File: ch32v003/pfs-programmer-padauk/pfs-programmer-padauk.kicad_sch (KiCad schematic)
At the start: 26 parts, among them J1 PGM1, J2 PGM2, J3 PGM, J4 USB_C_Receptacle_USB2.0, J5 HOLE, J6 HOLE, Q1 SI2301CDS-T1-GE3, Q2 2n7002, Q3 SI2301CDS-T1-GE3, Q4 2n7002, U1 CH32V003F4U6, U3 XC6206P332

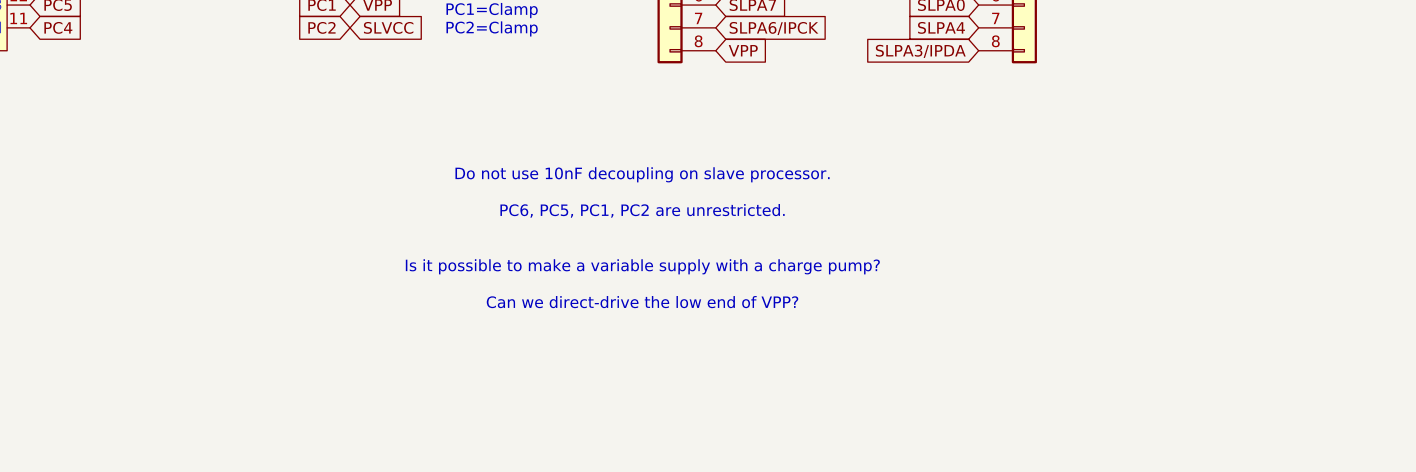
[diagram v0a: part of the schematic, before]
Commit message: Update with notes about charge pumps
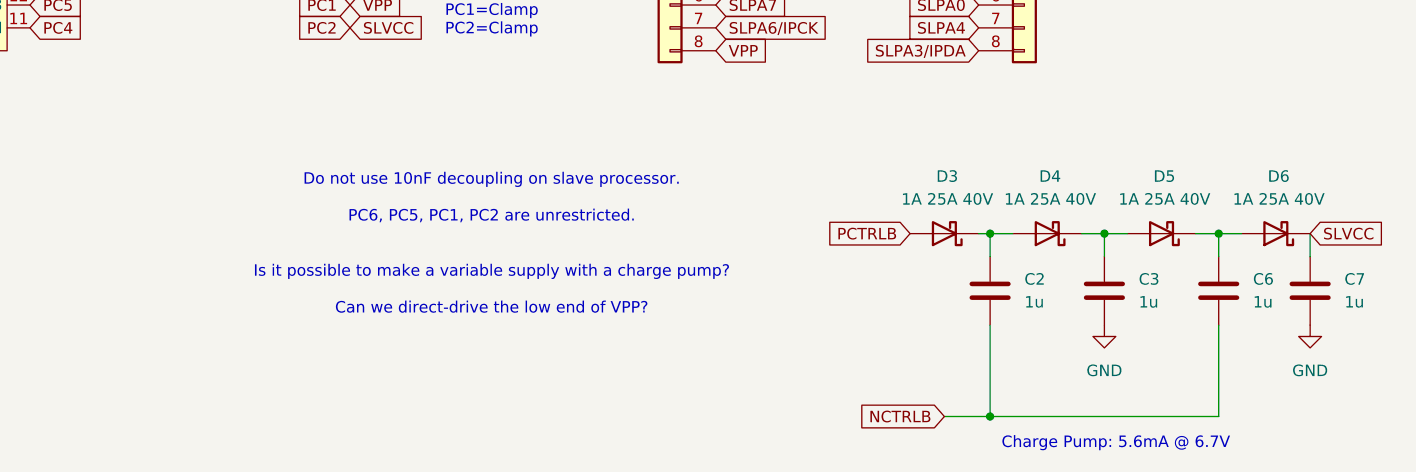
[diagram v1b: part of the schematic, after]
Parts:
- added C2, C3, C6, C7: 1u, Capacitor_SMD:C_0402_1005Metric, symbol Device:C
- added D3, D4, D5, D6: 1A 25A 40V, Diode_SMD:D_SOD-323_HandSoldering, symbol Device:D_Schottky
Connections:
- net GND: now also C3.2, C7.2
- net NCTRLB: now also C2.2, C6.2
- net PC2: now also C7.1, D6.1 (K)
- net PCTRLB: now also D3.2 (A)
- new net: C3.1, D4.1 (K), D5.2 (A)
- new net: C2.1, D3.1 (K), D4.2 (A)
- new net: C6.1, D5.1 (K), D6.2 (A)
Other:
- note added: "Charge Pump: 5.6mA @ 6.7V"
